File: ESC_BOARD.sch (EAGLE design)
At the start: 37 parts, among them J5 284512-3-180, J6 284512-3-180, J7 284512-3-180, J8 284512-3-180, U1 SN74CBTLV3257PWR, Y1 ECS-80-S-4X

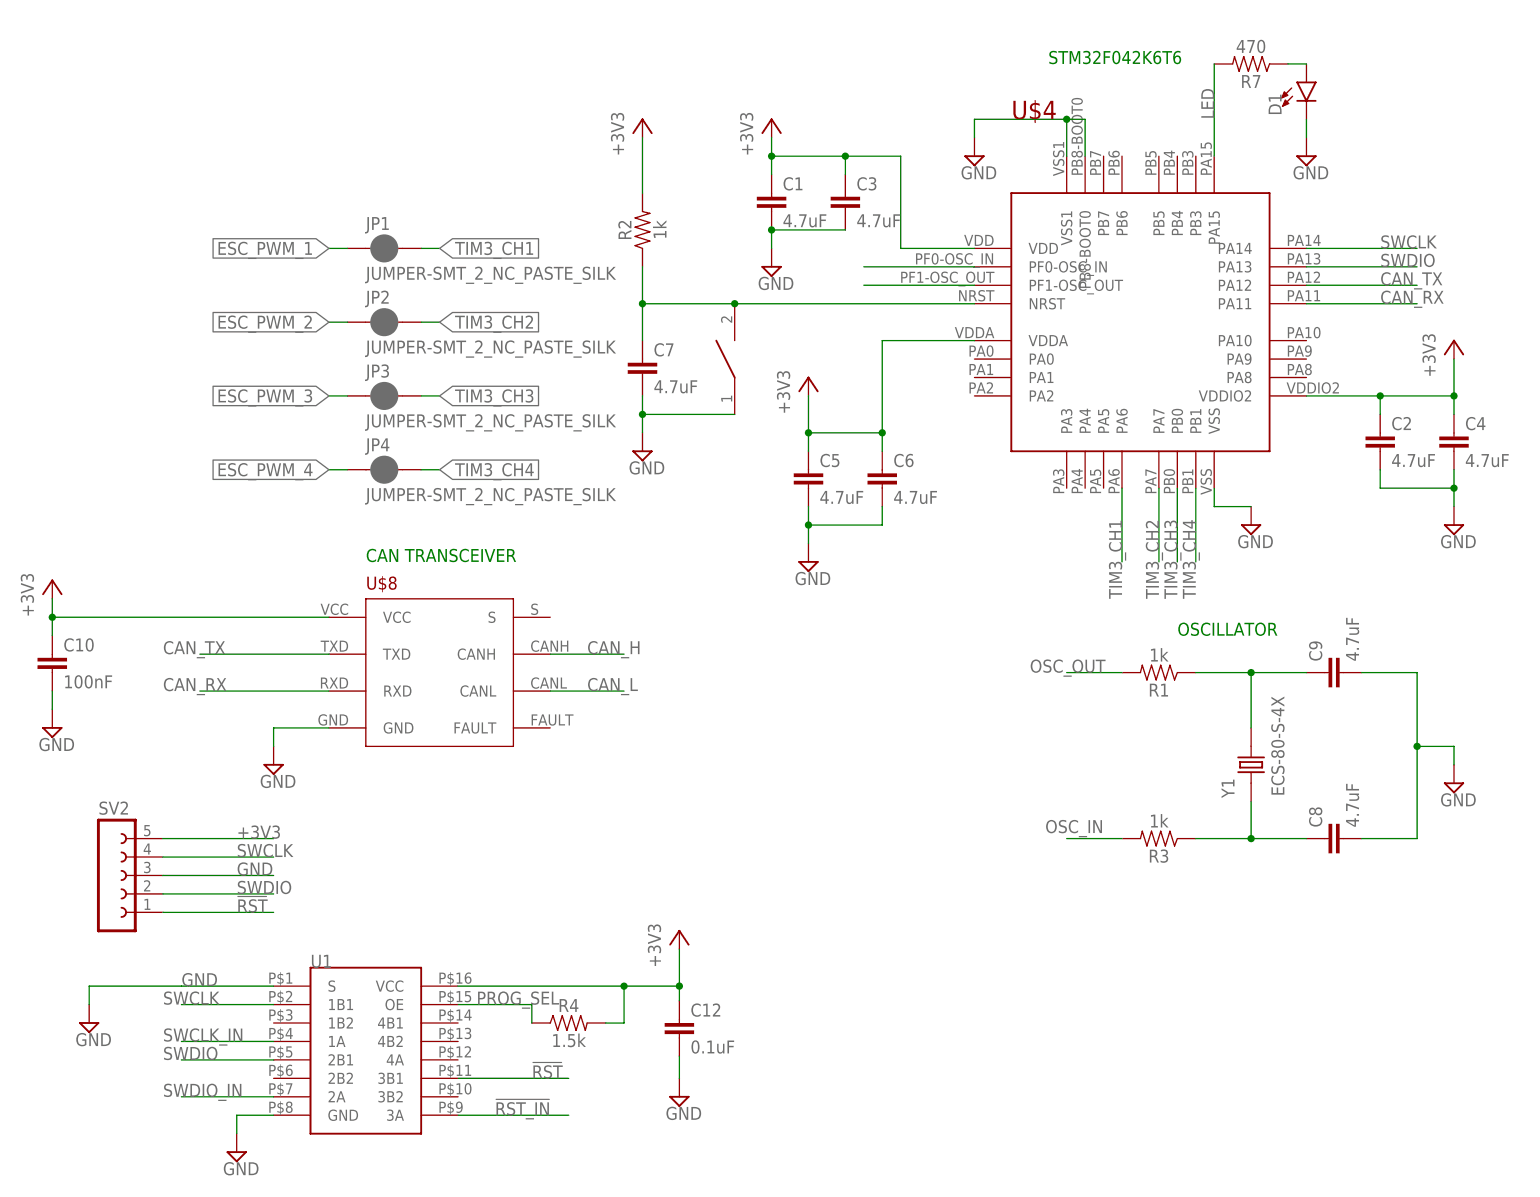
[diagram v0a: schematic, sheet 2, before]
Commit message: resistor ID added and changed SWD connections
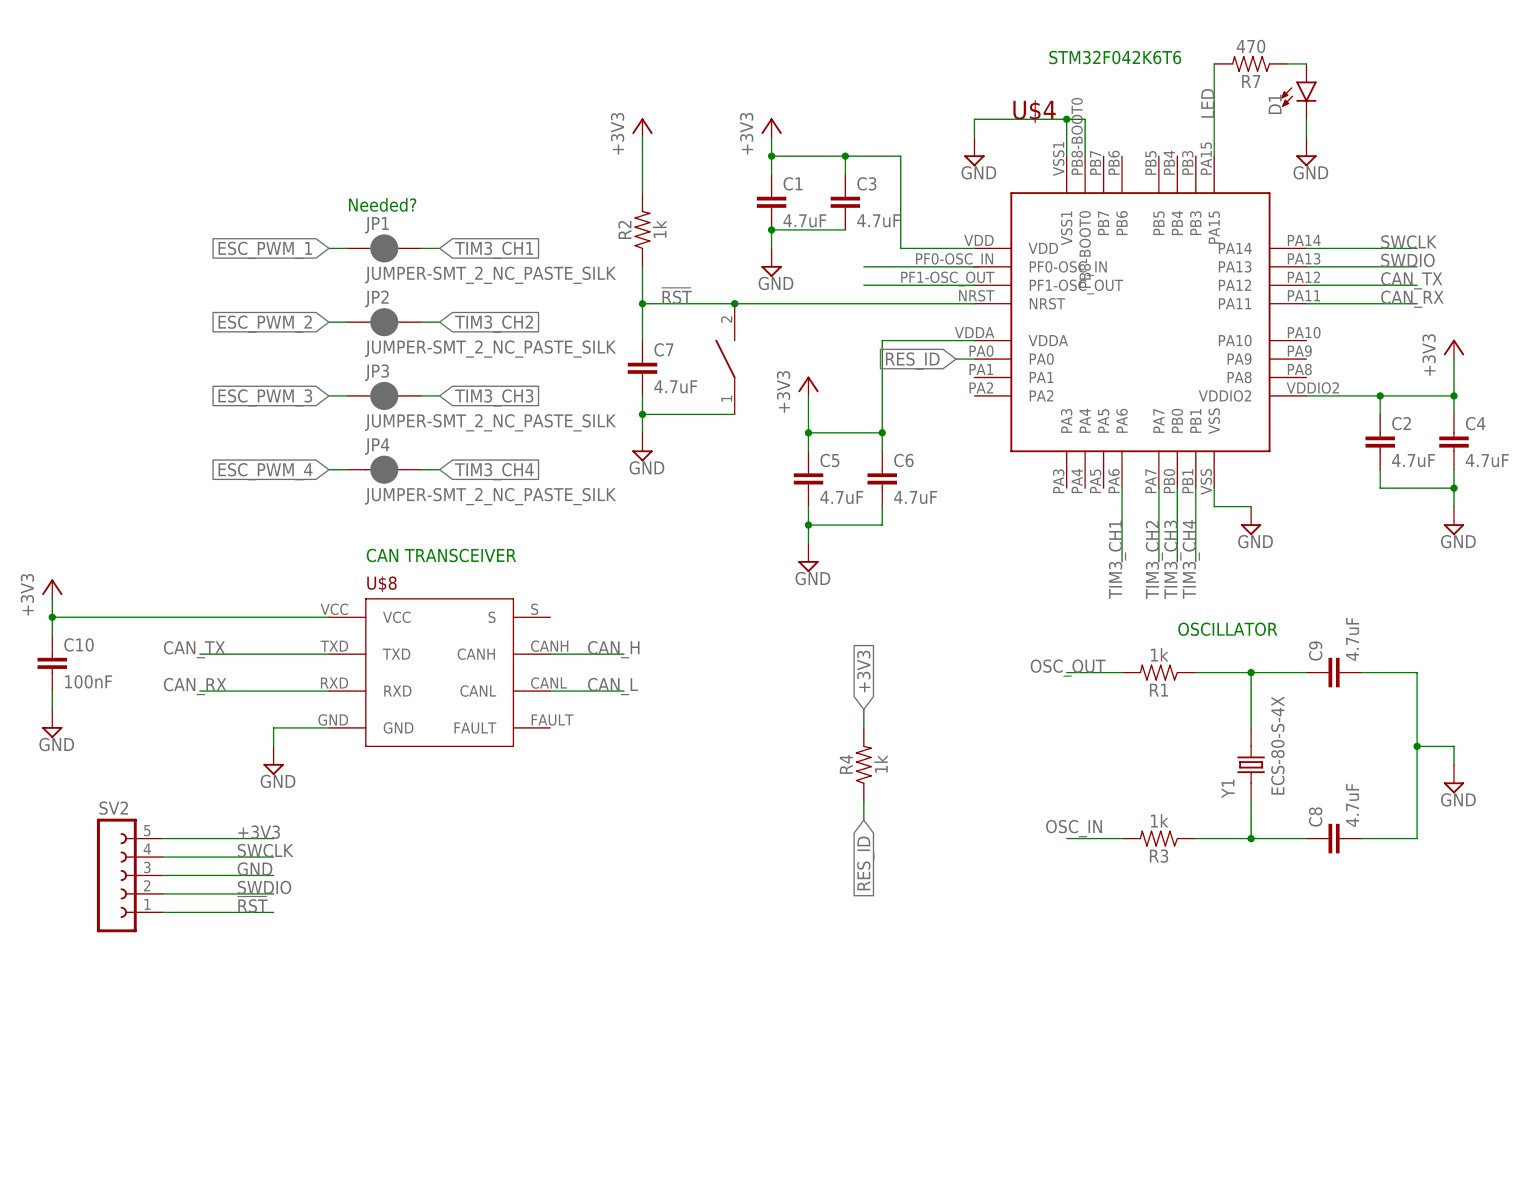
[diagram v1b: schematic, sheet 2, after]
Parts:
- removed C12: 0.1uF, SparkFun-Capacitors:0.1UF-0603-25V-(+80/-20%)
- removed U1: SN74CBTLV3257PWR, SN74CBTLV3257PWR:SN74CBTLV3257PWR
- R4: value 1.5k -> 1k; device SparkFun-Resistors:1.5KOHM-0603-1/10W-1% -> SparkFun-Resistors:1KOHM-0603-1/10W-1%
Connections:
- removed net !RST_IN: U$1G$1.P$20, U1.3A
- removed net NRST1: C7.1, R2.1, RESET.P$2, U$4.NRST
- removed net PROG_SEL: R4.1, U$1G$1.P$5, U1.OE
- removed net SWCLK_IN: U$1G$1.P$22, U1.1A
- removed net SWDIO_IN: U$1G$1.P$21, U1.2A
- new net RES_ID: R4.1, U$1G$1.P$19, U$4.PA0
- net !RST: now also C7.1, R2.1, RESET.P$2, U$1G$1.P$20, U$4.NRST; no longer U1.3B1
- net +3V3: no longer C12.1, U1.VCC
- net GND: no longer C12.2, U1.GND, U1.S
- net SWCLK: now also U$1G$1.P$22; no longer U1.1B1
- net SWDIO: now also U$1G$1.P$21; no longer U1.2B1
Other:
- note added: "Needed?"
- moved on the sheet: R4

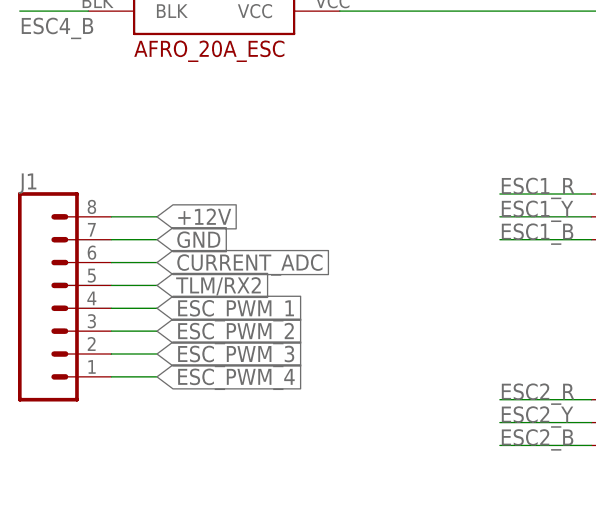
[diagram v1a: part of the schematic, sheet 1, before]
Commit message: placed most components
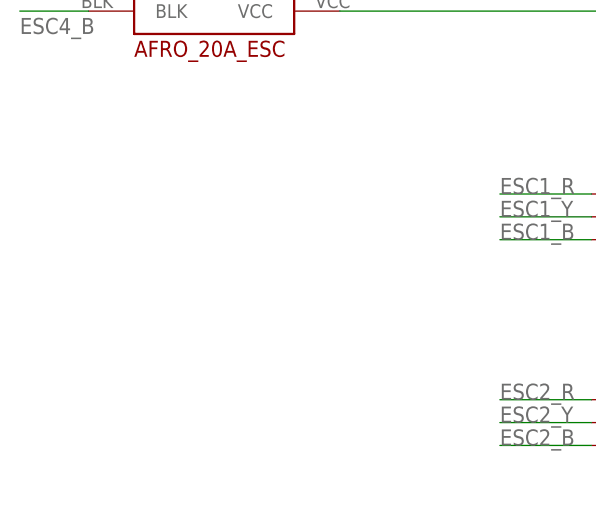
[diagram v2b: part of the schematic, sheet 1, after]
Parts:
- removed C3: 4.7uF, SparkFun-Capacitors:4.7UF0603
- removed J1: (no value), SparkFun-Connectors:CONN_08"
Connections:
- removed net CURRENT_ADC: J1.6
- removed net TLM/RX2: J1.5
- net +12V: no longer J1.8
- net +3V3: no longer C3.1
- net ESC_PWM_1: no longer J1.4
- net ESC_PWM_2: no longer J1.3
- net ESC_PWM_3: no longer J1.2
- net ESC_PWM_4: no longer J1.1
- net GND: no longer C3.2, J1.7
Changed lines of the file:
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@@
 <part name="C1" library="SparkFun-Capacitors" library_urn="urn:adsk.eagle:library:510" deviceset="4.7UF" device="0603" package3d_urn="urn:adsk.eagle:package:37414/1" value="4.7uF"/>
 <part name="C2" library="SparkFun-Capacitors" library_urn="urn:adsk.eagle:library:510" deviceset="4.7UF" device="0603" package3d_urn="urn:adsk.eagle:package:37414/1" value="4.7uF"/>
-<part name="C3" library="SparkFun-Capacitors" library_urn="urn:adsk.eagle:library:510" deviceset="4.7UF" device="0603" package3d_urn="urn:adsk.eagle:package:37414/1" value="4.7uF"/>
 <part name="C4" library="SparkFun-Capacitors" library_urn="urn:adsk.eagle:library:510" deviceset="4.7UF" device="0603" package3d_urn="urn:adsk.eagle:package:37414/1" value="4.7uF"/>
 <part name="C5" library="SparkFun-Capacitors" library_urn="urn:adsk.eagle:library:510" deviceset="4.7UF" device="0603" package3d_urn="urn:adsk.eagle:package:37414/1" value="4.7uF"/>
@@
 <part name="J7" library="TE 3 pin 3.5mm" deviceset="284512-3-180" device=""/>
 <part name="J8" library="TE 3 pin 3.5mm" deviceset="284512-3-180" device=""/>
-<part name="J1" library="SparkFun-Connectors" library_urn="urn:adsk.eagle:library:513" deviceset="CONN_08" device="&quot;" package3d_urn="urn:adsk.eagle:package:38138/1"/>
 <part name="R4" library="SparkFun-Resistors" library_urn="urn:adsk.eagle:library:532" deviceset="1KOHM" device="-0603-1/10W-1%" package3d_urn="urn:adsk.eagle:package:39650/1" value="1k"/>
 </parts>
@@
 <attribute name="NAME" x="134.12" y="30.48" size="1.778" layer="95"/>
 <attribute name="VALUE" x="134.62" y="17.78" size="1.778" layer="96"/>
-</instance>
-<instance part="J1" gate="G$1" x="22.86" y="38.1" smashed="yes">
-<attribute name="VALUE" x="17.78" y="25.654" size="1.778" layer="96" font="vector"/>
-<attribute name="NAME" x="17.78" y="51.308" size="1.778" layer="95" font="vector"/>
 </instance>
 </instances>
@@
 <wire x1="185.42" y1="83.82" x2="185.42" y2="81.28" width="0.1524" layer="91"/>
 <junction x="198.12" y="83.82"/>
-</segment>
-<segment>
-<pinref part="J1" gate="G$1" pin="7"/>
-<wire x1="27.94" y1="45.72" x2="33.02" y2="45.72" width="0.1524" layer="91"/>
-<label x="33.02" y="45.72" size="1.778" layer="95" xref="yes"/>
 </segment>
 <segment>
@@
 </segment>
 <segment>
-<pinref part="J1" gate="G$1" pin="8"/>
-<wire x1="27.94" y1="48.26" x2="33.02" y2="48.26" width="0.1524" layer="91"/>
-<label x="33.02" y="48.26" size="1.778" layer="95" xref="yes"/>
-</segment>
-<segment>
 <pinref part="U$1" gate="G$1" pin="P$27"/>
 <wire x1="236.22" y1="38.1" x2="241.3" y2="38.1" width="0.1524" layer="91"/>
@@
 <label x="63.5" y="154.94" size="1.778" layer="95"/>
 </segment>
-<segment>
-<pinref part="J1" gate="G$1" pin="4"/>
-<wire x1="27.94" y1="38.1" x2="33.02" y2="38.1" width="0.1524" layer="91"/>
-<label x="33.02" y="38.1" size="1.778" layer="95" xref="yes"/>
-</segment>
 </net>
 <net name="ESC_PWM_2" class="1">
@@
 <label x="63.5" y="129.54" size="1.778" layer="95"/>
 </segment>
-<segment>
-<pinref part="J1" gate="G$1" pin="3"/>
-<wire x1="27.94" y1="35.56" x2="33.02" y2="35.56" width="0.1524" layer="91"/>
-<label x="33.02" y="35.56" size="1.778" layer="95" xref="yes"/>
-</segment>
 </net>
 <net name="ESC_PWM_3" class="1">
@@
 <label x="63.5" y="101.6" size="1.778" layer="95"/>
 </segment>
-<segment>
-<pinref part="J1" gate="G$1" pin="2"/>
-<wire x1="27.94" y1="33.02" x2="33.02" y2="33.02" width="0.1524" layer="91"/>
-<label x="33.02" y="33.02" size="1.778" layer="95" xref="yes"/>
-</segment>
 </net>
 <net name="ESC_PWM_4" class="1">
@@
 <label x="63.5" y="73.66" size="1.778" layer="95"/>
 </segment>
-<segment>
-<pinref part="J1" gate="G$1" pin="1"/>
-<wire x1="27.94" y1="30.48" x2="33.02" y2="30.48" width="0.1524" layer="91"/>
-<label x="33.02" y="30.48" size="1.778" layer="95" xref="yes"/>
-</segment>
 </net>
 <net name="SWDIO" class="1">
@@
 <wire x1="236.22" y1="73.66" x2="238.76" y2="73.66" width="0.1524" layer="91"/>
 <label x="238.76" y="73.66" size="1.778" layer="95" xref="yes"/>
-</segment>
-</net>
-<net name="TLM/RX2" class="1">
-<segment>
-<pinref part="J1" gate="G$1" pin="5"/>
-<wire x1="27.94" y1="40.64" x2="33.02" y2="40.64" width="0.1524" layer="91"/>
-<label x="33.02" y="40.64" size="1.778" layer="95" xref="yes"/>
-</segment>
-</net>
-<net name="CURRENT_ADC" class="1">
-<segment>
-<pinref part="J1" gate="G$1" pin="6"/>
-<wire x1="27.94" y1="43.18" x2="33.02" y2="43.18" width="0.1524" layer="91"/>
-<label x="33.02" y="43.18" size="1.778" layer="95" xref="yes"/>
 </segment>
 </net>
@@
 <attribute name="VALUE" x="204.724" y="109.601" size="1.778" layer="96" font="vector"/>
 </instance>
-<instance part="C3" gate="G$1" x="129.54" y="144.78" smashed="yes">
-<attribute name="NAME" x="131.064" y="147.701" size="1.778" layer="95" font="vector"/>
-<attribute name="VALUE" x="131.064" y="142.621" size="1.778" layer="96" font="vector"/>
-</instance>
 <instance part="C4" gate="G$1" x="213.36" y="111.76" smashed="yes">
 <attribute name="NAME" x="214.884" y="114.681" size="1.778" layer="95" font="vector"/>
@@
 <pinref part="GND" gate="GND" pin="GND"/>
 <wire x1="119.38" y1="142.24" x2="119.38" y2="139.7" width="0.1524" layer="91"/>
-<pinref part="C3" gate="G$1" pin="2"/>
-<wire x1="119.38" y1="142.24" x2="129.54" y2="142.24" width="0.1524" layer="91"/>
-<junction x="119.38" y="142.24"/>
 </segment>
 <segment>
@@
 <pinref part="+3V1" gate="G$1" pin="+3V3"/>
 <wire x1="119.38" y1="154.94" x2="119.38" y2="152.4" width="0.1524" layer="91"/>
-<wire x1="119.38" y1="152.4" x2="129.54" y2="152.4" width="0.1524" layer="91"/>
-<pinref part="C3" gate="G$1" pin="1"/>
-<wire x1="129.54" y1="152.4" x2="129.54" y2="149.86" width="0.1524" layer="91"/>
+<wire x1="119.38" y1="152.4" x2="137.16" y2="152.4" width="0.1524" layer="91"/>
 <pinref part="C1" gate="G$1" pin="1"/>
 <wire x1="119.38" y1="149.86" x2="119.38" y2="152.4" width="0.1524" layer="91"/>
@@
 <wire x1="147.32" y1="139.7" x2="137.16" y2="139.7" width="0.1524" layer="91"/>
 <wire x1="137.16" y1="139.7" x2="137.16" y2="152.4" width="0.1524" layer="91"/>
-<wire x1="137.16" y1="152.4" x2="129.54" y2="152.4" width="0.1524" layer="91"/>
-<junction x="129.54" y="152.4"/>
-</segment>
-<segment>
+</segment>
+<segment>

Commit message: routed for rev2
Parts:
- removed D1: (no value), SparkFun-LED:LED0603
- removed RESET: SWITCH, DiscreteComponents:SWITCH
- added U$2: MURATA-DC-DC, MURATA_3pin_dcdc:MURATA-DC-DC
- added U$3: DISCRETECOMPONENTS_SWITCH, Push button - FSM2JMTR:DISCRETECOMPONENTS_SWITCH
- added U$5: LED-0805, LED-0805:LED-0805
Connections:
- net !RST: now also U$3.P$2; no longer RESET.P$2
- net +12V: now also U$2.VIN
- net +3V3: now also U$2.VOUT
- net ESC1_B: now also J5.1; no longer J5.3
- net ESC1_R: now also J5.3; no longer J5.1
- net ESC2_B: now also J6.1; no longer J6.3
- net ESC2_R: now also J6.3; no longer J6.1
- net GND: now also U$2.GND, U$3.P$1, U$5.C; no longer D1.C, RESET.P$1
- net N$24: now also U$5.A; no longer D1.A
- net TIM3_CH1: now also U$4.PA7; no longer U$4.PA6
- net TIM3_CH2: now also U$4.PA6; no longer U$4.PA7
- net TIM3_CH3: now also U$4.PB1; no longer U$4.PB0
- net TIM3_CH4: now also U$4.PB0; no longer U$4.PB1
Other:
- note added: "Populate with female headers"

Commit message: connector CAD and a few touchups
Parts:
- removed J5, J6, J7, J8: 284512-3-180, TE 3 pin 3.5mm:284512-3-180
- removed U$1: ESC2BACKPLANE, ESC_to_Backplane_Connectors:ESC2BACKPLANE
- added J1, J2, J3, J4: TE_2351886-3-(VERT), TE 3 pin 3.5mm:TE_2351886-3-(VERT)
- added U$6: ESC2BACKPLANE, ESC_to_Backplane_Connectors_esc:ESC2BACKPLANE
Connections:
- net !RST: now also U$6G$1.P$20; no longer U$1G$1.P$20
- net +12V: now also U$6G$1.P$10, U$6G$1.P$11, U$6G$1.P$12, U$6G$1.P$13, U$6G$1.P$23, U$6G$1.P$24, U$6G$1.P$25, U$6G$1.P$26, U$6G$1.P$27, U$6G$1.P$9, U$6G$2.P$A, U$6G$2.P$B, U$6G$2.P$C, U$6G$2.P$D, U$6G$2.P$E, U$6G$2.P$O, U$6G$2.P$P, U$6G$2.P$Q, U$6G$2.P$R, U$6G$2.P$S; no longer U$1G$1.P$10, U$1G$1.P$11, U$1G$1.P$12, U$1G$1.P$13, U$1G$1.P$23, U$1G$1.P$24, U$1G$1.P$25, U$1G$1.P$26, U$1G$1.P$27, U$1G$1.P$9, U$1G$2.P$A, U$1G$2.P$B, U$1G$2.P$C, U$1G$2.P$D, U$1G$2.P$E, U$1G$2.P$O, U$1G$2.P$P, U$1G$2.P$Q, U$1G$2.P$R, U$1G$2.P$S
- net +3V3: now also U$6G$2.P$G, U$6G$2.P$H, U$6G$2.P$U, U$6G$2.P$V; no longer U$1G$2.P$G, U$1G$2.P$H, U$1G$2.P$U, U$1G$2.P$V
- net CAN_H: now also U$6G$1.P$6; no longer U$1G$1.P$6
- net CAN_L: now also U$6G$1.P$7; no longer U$1G$1.P$7
- net ESC1_B: now also J1.1; no longer J5.1
- net ESC1_R: now also J1.3; no longer J5.3
- net ESC1_Y: now also J1.2; no longer J5.2
- net ESC2_B: now also J4.1; no longer J6.1
- net ESC2_R: now also J4.3; no longer J6.3
- net ESC2_Y: now also J4.2; no longer J6.2
- net ESC3_B: now also J2.1; no longer J7.1
- net ESC3_R: now also J2.3; no longer J7.3
- net ESC3_Y: now also J2.2; no longer J7.2
- net ESC4_B: now also J3.1; no longer J8.1
- net ESC4_R: now also J3.3; no longer J8.3
- net ESC4_Y: now also J3.2; no longer J8.2
- net GND: now also U$6G$1.P$1, U$6G$1.P$15, U$6G$1.P$16, U$6G$1.P$17, U$6G$1.P$18, U$6G$1.P$2, U$6G$1.P$3, U$6G$1.P$4, U$6G$2.P$AA, U$6G$2.P$BB, U$6G$2.P$J, U$6G$2.P$K, U$6G$2.P$L, U$6G$2.P$M, U$6G$2.P$N, U$6G$2.P$X, U$6G$2.P$Y, U$6G$2.P$Z; no longer U$1G$1.P$1, U$1G$1.P$15, U$1G$1.P$16, U$1G$1.P$17, U$1G$1.P$18, U$1G$1.P$2, U$1G$1.P$3, U$1G$1.P$4, U$1G$2.P$AA, U$1G$2.P$BB, U$1G$2.P$J, U$1G$2.P$K, U$1G$2.P$L, U$1G$2.P$M, U$1G$2.P$N, U$1G$2.P$X, U$1G$2.P$Y, U$1G$2.P$Z
- net RES_ID: now also U$6G$1.P$19; no longer U$1G$1.P$19
- net SWCLK: now also U$6G$1.P$22; no longer U$1G$1.P$22
- net SWDIO: now also U$6G$1.P$21; no longer U$1G$1.P$21
